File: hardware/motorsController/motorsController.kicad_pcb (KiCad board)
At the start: 2 copper layers, 166.1 x 53.6 mm, 47 parts, among them J1 batery_connector, J10 batery_connector, J2 Screw_Terminal_01x01, J3 Screw_Terminal_01x01, J4 Screw_Terminal_01x01, J5 Screw_Terminal_01x01, J6 Screw_Terminal_01x01, J7 Screw_Terminal_01x01, J8 Screw_Terminal_01x01, J9 Screw_Terminal_01x01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

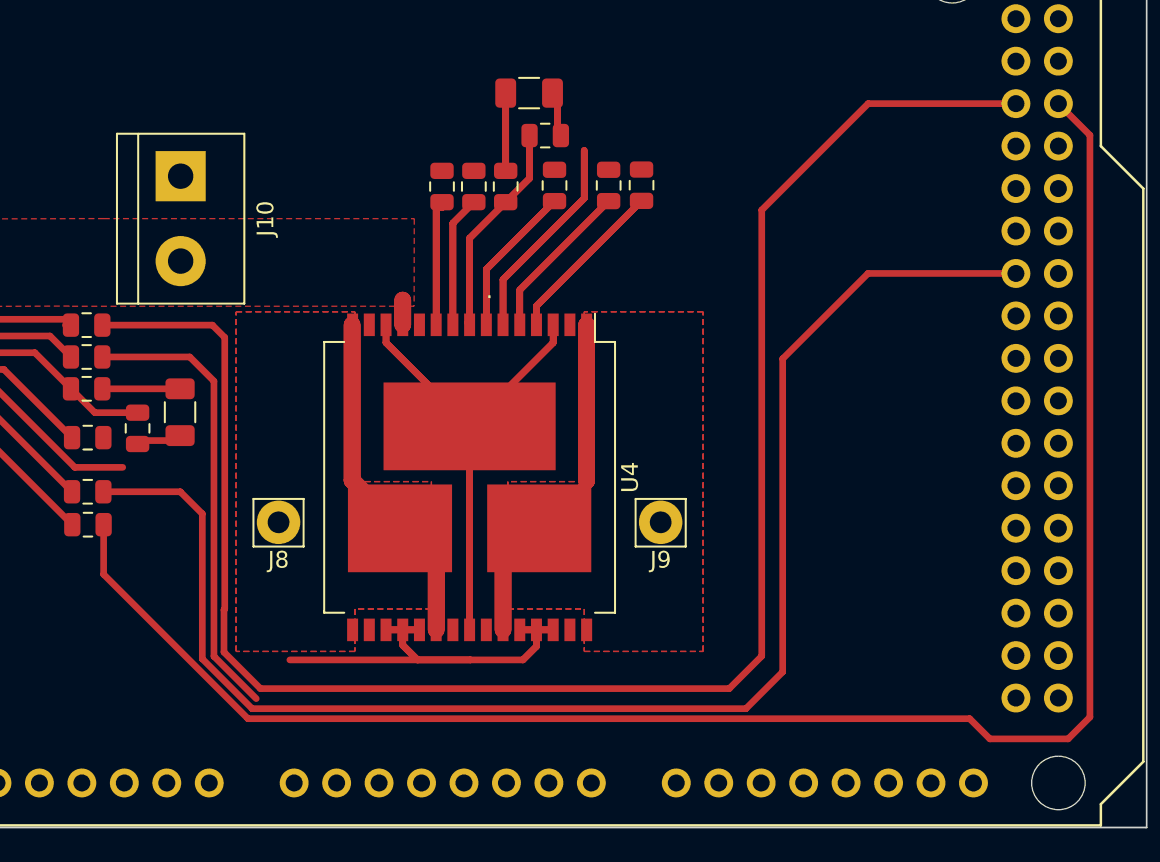
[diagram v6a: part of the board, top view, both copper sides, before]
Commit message: connect right-rear driver to arduino
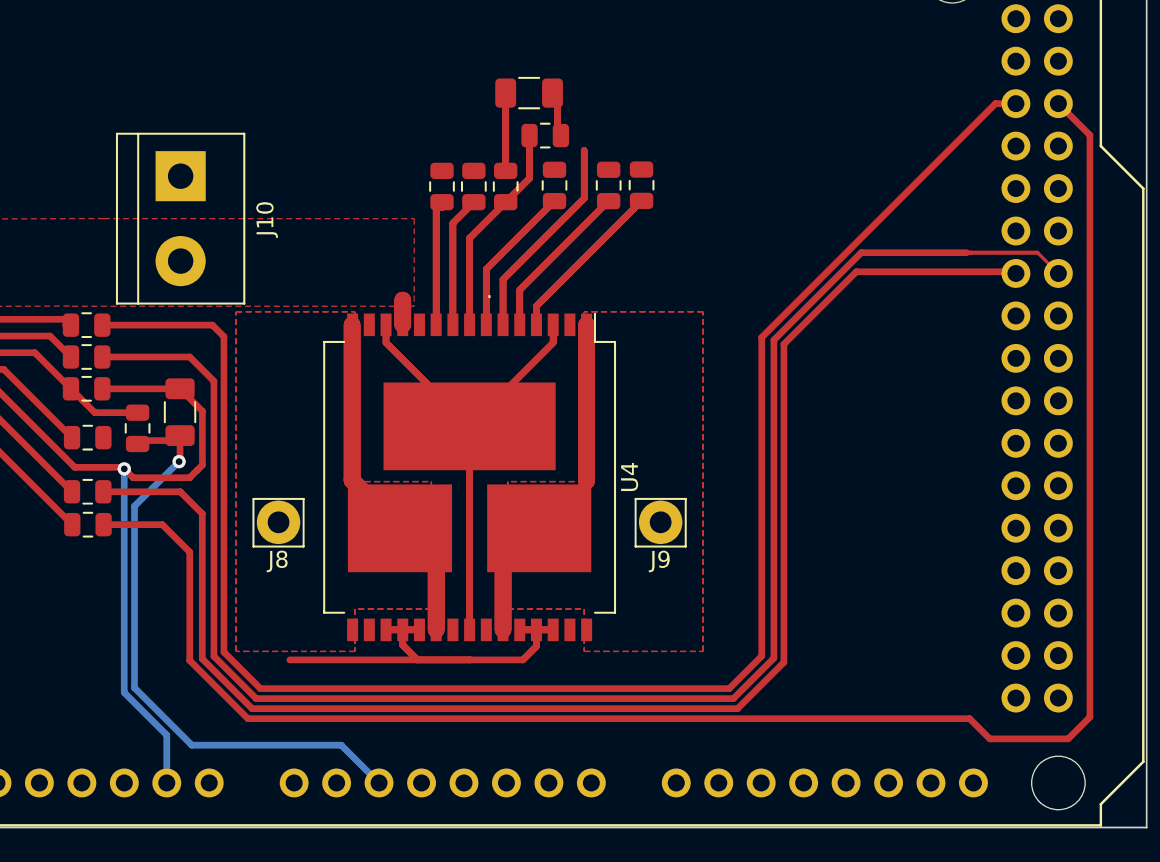
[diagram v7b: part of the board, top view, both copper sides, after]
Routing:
- net /motor_right_rear_diag_b: track 27.3 -> 98.0 mm
- net /motor_right_rear_cs: track 2.66 -> 35.9 mm, vias 0 -> 1
- net GND: track 225.3 -> 255.5 mm, vias 0 -> 1
- net /motor_right_rear_back: track 104.9 -> 100.4 mm
- net /motor_right_rear_fwd: track 104.1 -> 106.1 mm

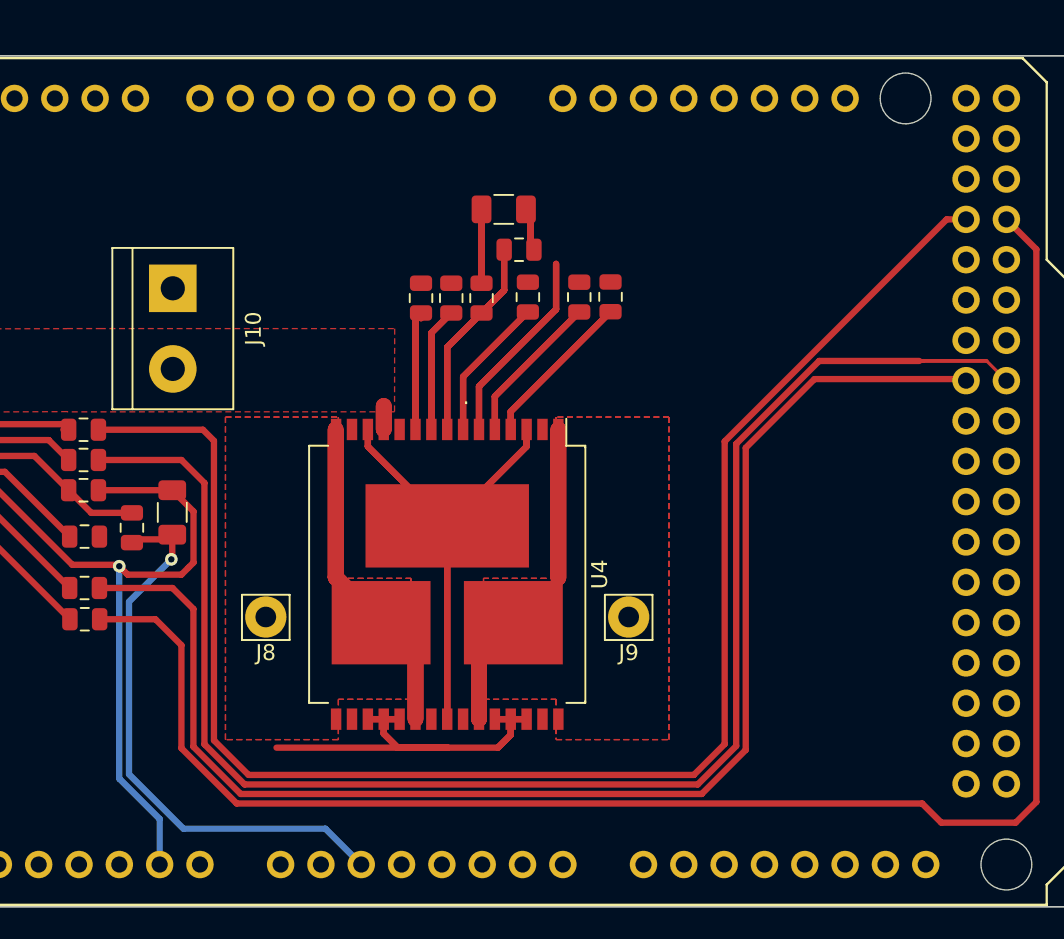
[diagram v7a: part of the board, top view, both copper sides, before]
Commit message: connect left-rear driver to arduino
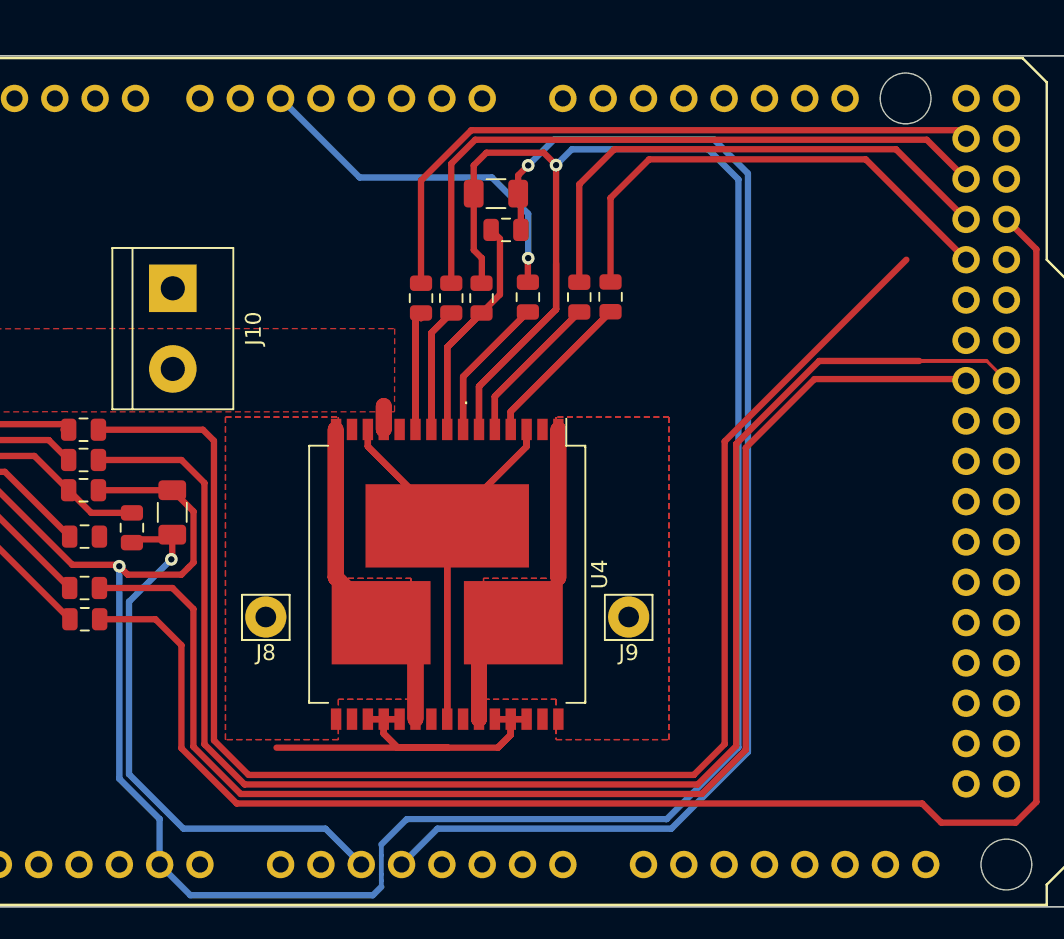
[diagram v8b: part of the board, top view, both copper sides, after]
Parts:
- moved R22 1.49 mm to (162.2, 35.3)
- moved C4 1.11 mm to (161.5, 33.0)
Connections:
- XA1 pad D22: /motor_right_front_back -> /motor_left_rear_back
- XA1 pad D24: /motor_left_front_back -> /motor_left_rear_diag_b
- XA1 pad D26: /motor_right_rear_back -> /motor_left_rear_diag_a
- XA1 pad D28: /motor_left_rear_back -> /motor_left_rear_fwd
- XA1 pad D29: /motor_left_rear_fwd -> /motor_right_rear_back
- XA1 pad D36: /motor_left_rear_diag_a -> Net-(XA1-PadD36)
- XA1 pad D37: /motor_left_rear_diag_b -> Net-(XA1-PadD37)
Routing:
- net GND: track 255.5 -> 357.1 mm, vias 1 -> 2
- net /motor_left_rear_cs: track 5.33 -> 81.2 mm, vias 0 -> 1
- net /motor_left_rear_back: track 0.00 -> 42.3 mm
- net /motor_left_rear_diag_b: track 0.00 -> 41.6 mm
- net /motor_left_rear_diag_a: track 0.00 -> 33.6 mm
- net /motor_left_rear_fwd: track 0.00 -> 31.3 mm
- net /motor_left_rear_pwm: track 0.00 -> 22.9 mm, vias 0 -> 1
- net /motor_right_rear_back: track 100.4 -> 95.6 mm
- net Net-(R22-Pad1): track 26.5 -> 22.8 mm
